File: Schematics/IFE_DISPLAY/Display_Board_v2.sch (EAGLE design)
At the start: 55 parts, among them IC2 EP2C5T144, Q1 16MHz, Q3 16MHz, U2 EPCS1SI8N, U3 ATMEGA328P-AU, U4 HEX_CONVERTER, U5 HEX_CONVERTER, U6 MC78LC33NTRG, U7 MC78LC50NTRG

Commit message: adding linear regs
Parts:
- removed AS1, JTAG1: (no value), pinhead:PINHD-2X5
- removed C24: 220u, Capacitors:C1206
- removed R27, R28, R33: 1K, resistor:R-US_R0805
- removed U6: MC78LC33NTRG, ON Semiconductor_By_element14_Batch_1:MC78LC33NTRG
- removed U7: MC78LC50NTRG, ON Semiconductor_By_element14_Batch_1:MC78LC50NTRG
- added AS2, JTAG2: (no value), pinhead:PINHD-2X5
- added QG1: SM77H, crystal:SM77H
- added R11, R12, R2: 1K, resistor:R-US_R0805
- added R13, R14, R15, R16: 10K, resistor:R-US_R0805
- added U$6: 10CL006ZE144, Display_Custom:10CL006ZE144
- added U$7: EPCQ16A, Display_Custom:EPCQ16A
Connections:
- new net N$10: R13.1, U$6.NSTATUS
- new net N$11: U$6.VCC_PLL1@37, U$6.VCC_PLL2@109
- new net N$12: U$6.DCLK
- new net N$14: U$6.DATA1,ASDO
- new net N$15: U$6.MSEL0
- new net N$8: U$6.MSEL2
- new net N$9: U$6.VCCA1@35, U$6.VCCA2@107
- net +12V: no longer C24.1, U6.VIN, U7.VIN
- net +3V3: now also AS2.4, JTAG2.4, QG1.VCC, R11.1, R12.2, R13.2, R14.2, R15.2, U$6.VCC@117, U$6.VCC@122, U$6.VCC@130, U$6.VCC@139, U$6.VCC@17, U$6.VCC@26, U$6.VCC@40, U$6.VCC@47, U$6.VCC@56, U$6.VCC@62, U$6.VCC@81, U$6.VCC@93, U$7.VCC; no longer AS1.4, JTAG1.4, R28.1, R33.2, U6.VOUT
- net +5V: no longer U7.VOUT
- net 50_MHZ: now also QG1.OUT, U$6.CLK0
- net ASDO: now also AS2.9, U$7.DATA1; no longer AS1.9
- net CONF_DONE: now also AS2.3, R15.1, U$6.CONF_DONE; no longer AS1.3
- net DATA0: now also AS2.7, U$7.DATA0; no longer AS1.7
- net DCLK: now also AS2.1, U$7.DCLK; no longer AS1.1
- net GND: now also AS2.10, AS2.2, JTAG2.10, JTAG2.2, QG1.GND, R16.2, R2.1, U$6.GND@104, U$6.GND@108, U$6.GND@110, U$6.GND@118, U$6.GND@123, U$6.GND@131, U$6.GND@140, U$6.GND@19, U$6.GND@27, U$6.GND@30, U$6.GND@36, U$6.GND@4, U$6.GND@41, U$6.GND@48, U$6.GND@57, U$6.GND@63, U$6.GND@64, U$6.GND@79, U$6.GND@82, U$6.GND@95, U$6.MSEL1, U$7.GND; no longer AS1.10, AS1.2, C24.2, JTAG1.10, JTAG1.2, R27.1, U6.GND, U7.GND
- net NCE: now also AS2.6, R16.1, U$6.NCE; no longer AS1.6
- net NCONFIG: now also AS2.5, R14.1, U$6.NCONFIG; no longer AS1.5
- net NCSO: now also AS2.8, U$6.FLASH_NCE,NCSO, U$7.NCS; no longer AS1.8
- net TCK: now also JTAG2.1, R2.2; no longer JTAG1.1, R27.2
- net TDI: now also JTAG2.9, R11.2; no longer JTAG1.9, R28.2
- net TDO: now also JTAG2.3; no longer JTAG1.3
- net TMS: now also JTAG2.5, R12.1; no longer JTAG1.5, R33.1
- net VCC: now also U$6.VINT@102, U$6.VINT@116, U$6.VINT@134, U$6.VINT@29, U$6.VINT@45, U$6.VINT@5, U$6.VINT@61, U$6.VINT@78

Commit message: Working on adding 2.5V for the PLL
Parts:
- added U$8: LF33ABDT-TR, Display_Custom:LF33ABDT-TR
- added U$9: L7805CDT-TR, Display_Custom:L7805CDT-TR
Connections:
- net +12V: now also U$8.VIN, U$9.VIN
- net +3V3: now also U$8.VOUT
- net +5V: now also U$9.VOUT
- net GND: now also U$8.GND, U$9.GND
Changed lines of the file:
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@@
 <?xml version="1.0" encoding="utf-8"?>
 <!DOCTYPE eagle SYSTEM "eagle.dtd">
-<eagle version="8.6.0">
+<eagle version="8.6.3">
 <drawing>
 <settings>
@@
 <part name="GND22" library="supply1" library_urn="urn:adsk.eagle:library:371" deviceset="GND" device=""/>
 <part name="ANDREWSMITH" library="frames" library_urn="urn:adsk.eagle:library:229" deviceset="A3L-LOC" device=""/>
+<part name="U$8" library="Display_Custom" deviceset="LF33ABDT-TR" device=""/>
+<part name="U$9" library="Display_Custom" deviceset="L7805CDT-TR" device=""/>
 </parts>
 <sheets>
@@
 <instance part="R3" gate="G$1" x="99.06" y="157.48" rot="R90"/>
 <instance part="P+1" gate="1" x="88.9" y="177.8"/>
+<instance part="U$8" gate="LF33ABDT" x="45.72" y="114.3"/>
+<instance part="U$9" gate="L7805" x="132.08" y="114.3"/>
 </instances>
 <busses>
@@
 </segment>
 <segment>
-<wire x1="114.3" y1="104.14" x2="109.22" y2="104.14" width="0.1524" layer="91"/>
 <wire x1="109.22" y1="104.14" x2="109.22" y2="101.6" width="0.1524" layer="91"/>
 <pinref part="GND14" gate="1" pin="GND"/>
@@
 <wire x1="109.22" y1="106.68" x2="109.22" y2="104.14" width="0.1524" layer="91"/>
 <junction x="109.22" y="104.14"/>
+<wire x1="132.08" y1="106.68" x2="132.08" y2="104.14" width="0.1524" layer="91"/>
+<wire x1="132.08" y1="104.14" x2="109.22" y2="104.14" width="0.1524" layer="91"/>
+<pinref part="U$9" gate="L7805" pin="GND"/>
 </segment>
 <segment>
@@
 <wire x1="22.86" y1="106.68" x2="22.86" y2="104.14" width="0.1524" layer="91"/>
 <wire x1="22.86" y1="104.14" x2="22.86" y2="101.6" width="0.1524" layer="91"/>
-<wire x1="27.94" y1="104.14" x2="22.86" y2="104.14" width="0.1524" layer="91"/>
 <junction x="22.86" y="104.14"/>
 <pinref part="GND20" gate="1" pin="GND"/>
+<wire x1="22.86" y1="104.14" x2="45.72" y2="104.14" width="0.1524" layer="91"/>
+<pinref part="U$8" gate="LF33ABDT" pin="GND"/>
+<wire x1="45.72" y1="104.14" x2="45.72" y2="106.68" width="0.1524" layer="91"/>
 </segment>
 <segment>
@@
 <net name="+3V3" class="0">
 <segment>
-<wire x1="63.5" y1="116.84" x2="68.58" y2="116.84" width="0.1524" layer="91"/>
 <pinref part="C12" gate="G$1" pin="1"/>
 <wire x1="68.58" y1="116.84" x2="68.58" y2="114.3" width="0.1524" layer="91"/>
@@
 <junction x="68.58" y="116.84"/>
 <pinref part="+3V3" gate="G$1" pin="+3V3"/>
+<pinref part="U$8" gate="LF33ABDT" pin="VOUT"/>
+<wire x1="68.58" y1="116.84" x2="58.42" y2="116.84" width="0.1524" layer="91"/>
 </segment>
 </net>
@@
 <segment>
 <pinref part="P+4" gate="1" pin="+5V"/>
-<wire x1="149.86" y1="116.84" x2="154.94" y2="116.84" width="0.1524" layer="91"/>
 <wire x1="154.94" y1="116.84" x2="154.94" y2="119.38" width="0.1524" layer="91"/>
 <pinref part="C5" gate="G$1" pin="1"/>
 <wire x1="154.94" y1="116.84" x2="154.94" y2="114.3" width="0.1524" layer="91"/>
 <junction x="154.94" y="116.84"/>
+<wire x1="144.78" y1="116.84" x2="154.94" y2="116.84" width="0.1524" layer="91"/>
+<pinref part="U$9" gate="L7805" pin="VOUT"/>
 </segment>
 <segment>
@@
 </segment>
 <segment>
-<wire x1="27.94" y1="116.84" x2="22.86" y2="116.84" width="0.1524" layer="91"/>
 <pinref part="C11" gate="G$1" pin="1"/>
 <wire x1="22.86" y1="116.84" x2="17.78" y2="116.84" width="0.1524" layer="91"/>
@@
 <pinref part="SUPPLY2" gate="+12V" pin="+12V"/>
 <wire x1="17.78" y1="119.38" x2="17.78" y2="116.84" width="0.1524" layer="91"/>
-</segment>
-<segment>
-<wire x1="114.3" y1="116.84" x2="109.22" y2="116.84" width="0.1524" layer="91"/>
+<pinref part="U$8" gate="LF33ABDT" pin="VIN"/>
+<wire x1="33.02" y1="116.84" x2="22.86" y2="116.84" width="0.1524" layer="91"/>
+</segment>
+<segment>
 <pinref part="C10" gate="G$1" pin="1"/>
 <wire x1="109.22" y1="116.84" x2="109.22" y2="114.3" width="0.1524" layer="91"/>
@@
 <pinref part="SUPPLY1" gate="+12V" pin="+12V"/>
 <wire x1="104.14" y1="119.38" x2="104.14" y2="116.84" width="0.1524" layer="91"/>
-</segment>
-<segment>
+<wire x1="109.22" y1="116.84" x2="119.38" y2="116.84" width="0.1524" layer="91"/>
+<pinref part="U$9" gate="L7805" pin="VIN"/>
+</segment>
+<segment>

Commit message: Finished power dist - Working on optimizing connections to FPGA
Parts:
- removed AS2, JTAG2: (no value), pinhead:PINHD-2X5
- removed IC2: EP2C5T144, altera-cyclone-II:EP2C5T144
- removed JP1: (no value), pinhead:PINHD-2X3
- removed LED1, LED2, LED3: (no value), led:LEDCHIP-LED0805
- removed QG1, QG2: SM77H, crystal:SM77H
- removed R29, R30, R31, R32: 10K, resistor:R-US_R0805
- removed U$1: 776280-1, IFE_AMPSEAL_Conn:776280-1
- removed U$4: ZIF40_0.5MM_PITCH, Connectors:ZIF40_0.5MM_PITCH
- removed U2: EPCS1SI8N, Altera_By_element14_Batch_1:EPCS1SI8N
- removed U3: ATMEGA328P-AU, Atmel_By_element14_Batch_1-00:ATMEGA328P-AU
- added 1.2T, 2.5T, 3.3T, 5T, DISP_A_T: TPTP12SQ, testpad:TPTP12SQ
- added 3.3V, 5V, FPGA, MICRO: (no value), led:LEDCHIP-LED0805
- added 50MHZ: SM77H, crystal:SM77H
- added AS, JTAG: (no value), pinhead:PINHD-2X5
- added ATMEGA328P: ATMEGA328P-AU, Atmel_By_element14_Batch_1-00:ATMEGA328P-AU
- added C14: 10u, rcl:C-EUC0805K
- added C15, C18, C19, C20, C21, C22, C23: 0.1u, rcl:C-EUC0805K
- added C16: 220uF, rcl:CPOL-USUD-6,3X7,7
- added C17: 1u, rcl:C-EUC0805K
- added DISPLAY: ZIF40_0.5MM_PITCH, Connectors:ZIF40_0.5MM_PITCH
- added ICP: (no value), pinhead:PINHD-2X3
- added R17: 127k, rcl:R-US_R0805
- added R18: 121k, rcl:R-US_R0805
- added R19: 25, rcl:R-US_R0805
- added R20: 330, resistor:R-US_R0805
- added TE_AMPSEAL_8: 776280-1, IFE_AMPSEAL_Conn:776280-1
- added U$10: TPS72101DBVT, Display_Custom:TPS72101DBVT
- added U$11: TPS6104X, Display_Custom:TPS6104X
- added U$13: SMAZ24-13-F, Display_Custom:SMAZ24-13-F
- added U$14: BAT54WS-7-F, Display_Custom:BAT54WS-7-F
- C1: value 1uF -> 0.1u
- C10, C11: value 0.1u -> 10u
- C13: value 10uF -> 10u; device microbuilder:CAP_CERAMIC_0805MP -> rcl:C-EUC0805K
- C2: value 1uF -> 10u
- L1: value 6.8uH power L CID 2276 -> 6.8uH
- R3: value 10K -> 10k; device microbuilder:RESISTOR_0805MP -> rcl:R-US_R0805
- R5: value 100 -> 330
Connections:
- removed net N$14: U$6.DATA1,ASDO
- removed net N$15: U$6.MSEL0
- removed net N$21: IC2.NSTATUS, R29.1
- removed net PWR_IN_24: U$1.6
- new net N$19: R17.2, R18.1, U$10.N/C
- new net V+: 2.5T.TP, C15.1, R17.1, U$10.VOUT, U$6.MSEL0, U$6.MSEL2
- net +12V: now also C16.+
- net +3V3: now also 3.3T.TP, 50MHZ.VCC, AS.4, C18.1, C19.1, C20.1, DISPLAY.P$4, JTAG.4; no longer AS2.4, IC2.VCC@1, IC2.VCC@10, IC2.VCC@11, IC2.VCC@12, IC2.VCC@13, IC2.VCC@16, IC2.VCC@18, IC2.VCC@2, IC2.VCC@20, IC2.VCC@3, IC2.VCC@6, IC2.VCC@8, JTAG2.4, QG1.VCC, QG2.VCC, R29.2, R31.2, R32.2, R5.2, U$4.P$4, U2.VCC, U2.VCC_2, U2.VCC_3
- net +5V: now also 5T.TP, ATMEGA328P.AVCC, ATMEGA328P.VCC, ATMEGA328P.VCC_2, C14.1, ICP.2, R20.2, R3.1, R5.2, U$10.ENABLE, U$10.VIN, U$11.VIN; no longer JP1.2, R3.2, U3.AVCC, U3.VCC, U3.VCC_2
- net 50_MHZ: now also 50MHZ.OUT; no longer IC2.CLK0, QG1.OUT, QG2.OUT
- net ASDO: now also AS.9, U$6.DATA1,ASDO; no longer AS2.9, IC2.IO1, U2.ASDI
- net BLUE_0: now also DISPLAY.P$21, U$6.IO54; no longer IC2.IO52, U$4.P$21
- net BLUE_1: now also DISPLAY.P$22, U$6.IO55; no longer IC2.IO53, U$4.P$22
- net BLUE_2: now also DISPLAY.P$23, U$6.IO58; no longer IC2.IO55, U$4.P$23
- net BLUE_3: now also DISPLAY.P$24, U$6.IO59; no longer IC2.IO57, U$4.P$24
- net BLUE_4: now also DISPLAY.P$25, U$6.IO60; no longer IC2.IO58, U$4.P$25
- net BLUE_5: now also DISPLAY.P$26, U$6.IO65; no longer IC2.IO59, U$4.P$26
- net BLUE_6: now also DISPLAY.P$27, U$6.IO66; no longer IC2.IO60, U$4.P$27
- net BLUE_7: now also DISPLAY.P$28, U$6.IO67; no longer IC2.IO63, U$4.P$28
- net CANH: now also TE_AMPSEAL_8.5; no longer U$1.5
- net CANL: now also TE_AMPSEAL_8.8; no longer U$1.8
- net CONF_DONE: now also AS.3; no longer AS2.3, IC2.CONF_DONE, R32.1
- net DATA0: now also AS.7, U$6.DATA0; no longer AS2.7, IC2.DATA0, U2.DATA
- net DCLK: now also AS.1, U$6.DCLK; no longer AS2.1, IC2.DCLK, U2.DCLK
- net DISP_CLK: now also DISPLAY.P$30, U$6.IO68; no longer IC2.IO3, U$4.P$30
- net DISP_DEN: now also DISPLAY.P$34, U$6.IO72; no longer IC2.IO9, U$4.P$34
- net DISP_EN: now also DISPLAY.P$31, U$6.IO69; no longer IC2.IO4, U$4.P$31
- net DISP_HSYNC: now also DISPLAY.P$32, U$6.IO70; no longer IC2.IO7, U$4.P$32
- net DISP_LEDA: now also C17.1, DISPLAY.P$2, DISP_A_T.TP, U$13.C, U$14.C; no longer U$4.P$2
- net DISP_LEDK: now also DISPLAY.P$1, R19.1, U$11.FB; no longer U$4.P$1
- net DISP_PWM: now also ATMEGA328P.PB1, R3.2, U$11.ENABLE; no longer R3.1, U3.PB1
- net DISP_VSYNC: now also DISPLAY.P$33, U$6.IO71; no longer IC2.IO8, U$4.P$33
- net DISP_XL: now also DISPLAY.P$39, U$6.IO75; no longer U$4.P$39
- net DISP_XR: now also DISPLAY.P$37, U$6.IO73; no longer U$4.P$37
- net DISP_YD: now also DISPLAY.P$38, U$6.IO74; no longer U$4.P$38
- net DISP_YU: now also DISPLAY.P$40, U$6.IO76; no longer U$4.P$40
- net FPGA_D0_3_3: no longer IC2.IO75
- net FPGA_D1_3_3: no longer IC2.IO76
- net FPGA_D2_3_3: no longer IC2.IO79
- net FPGA_D3_3_3: no longer IC2.IO80
- net FPGA_DATA0: now also ATMEGA328P.PC0; no longer U3.PC0
- net FPGA_DATA1: now also ATMEGA328P.PC1; no longer U3.PC1
- net FPGA_DATA2: now also ATMEGA328P.PC2; no longer U3.PC2
- net FPGA_DATA3: now also ATMEGA328P.PC3; no longer U3.PC3
- net FPGA_R0_3_3: no longer IC2.IO81
- net FPGA_R1_3_3: no longer IC2.IO86
- net FPGA_R2_3_3: no longer IC2.IO87
- net FPGA_R3_3_3: no longer IC2.IO92
- net FPGA_REG0: now also ATMEGA328P.PD4; no longer U3.PD4
- net FPGA_REG1: now also ATMEGA328P.PD5; no longer U3.PD5
- net FPGA_REG2: now also ATMEGA328P.PD6; no longer U3.PD6
- net FPGA_REG3: now also ATMEGA328P.PD7; no longer U3.PD7
- net FPGA_REG_SEL: now also ATMEGA328P.PC4; no longer U3.PC4
- net FPGA_RSEL_3_3: no longer IC2.IO73
- net FPGA_WRITE: now also ATMEGA328P.PD3; no longer U3.PD3
- net FPGA_W_3_3: no longer IC2.IO74
- net GND: now also 3.3V.C, 50MHZ.GND, 5V.C, AS.10, AS.2, ATMEGA328P.GND, ATMEGA328P.GND_2, ATMEGA328P.GND_3, C14.2, C15.2, C16.-, C17.2, C18.2, C19.2, C20.2, C21.2, C22.2, C23.2, DISPLAY.P$29, DISPLAY.P$3, DISPLAY.P$36, ICP.6, JTAG.10, JTAG.2, R18.2, R19.2, TE_AMPSEAL_8.1, TE_AMPSEAL_8.3, TE_AMPSEAL_8.4, TE_AMPSEAL_8.6, TE_AMPSEAL_8.7, U$10.GND, U$11.GND, U$13.A; no longer AS2.10, AS2.2, IC2.GND@1, IC2.GND@10, IC2.GND@11, IC2.GND@12, IC2.GND@13, IC2.GND@14, IC2.GND@15, IC2.GND@16, IC2.GND@17, IC2.GND@18, IC2.GND@19, IC2.GND@2, IC2.GND@20, IC2.GND@21, IC2.GND@22, IC2.GND@23, IC2.GND@3, IC2.GND@4, IC2.GND@5, IC2.GND@6, IC2.GND@7, IC2.GND@8, IC2.GND@9, IC2.MSEL0, IC2.MSEL1, JP1.6, JTAG2.10, JTAG2.2, LED3.C, QG1.GND, QG2.GND, R30.2, U$1.4, U$4.P$29, U$4.P$3, U$4.P$36, U2.GND, U3.GND, U3.GND_2, U3.GND_3
- net GREEN_0: now also DISPLAY.P$13, U$6.IO43; no longer IC2.IO41, U$4.P$13
- net GREEN_1: now also DISPLAY.P$14, U$6.IO44; no longer IC2.IO42, U$4.P$14
- net GREEN_2: now also DISPLAY.P$15, U$6.IO46; no longer IC2.IO43, U$4.P$15
- net GREEN_3: now also DISPLAY.P$16, U$6.IO49; no longer IC2.IO44, U$4.P$16
- net GREEN_4: now also DISPLAY.P$17, U$6.IO50; no longer IC2.IO45, U$4.P$17
- net GREEN_5: now also DISPLAY.P$18, U$6.IO51; no longer IC2.IO47, U$4.P$18
- net GREEN_6: now also DISPLAY.P$19, U$6.IO52; no longer IC2.IO48, U$4.P$19
- net GREEN_7: now also DISPLAY.P$20, U$6.IO53; no longer IC2.IO51, U$4.P$20
- net LED1: now also FPGA.C, U$6.IO144; no longer IC2.IO129, LED1.C
- net LED2: now also ATMEGA328P.PB2, MICRO.C; no longer IC2.IO132, LED2.C
- net MISO: now also ATMEGA328P.PB4, ICP.1; no longer JP1.1, U3.PB4
- net MOSI: now also ATMEGA328P.PB3, ICP.4; no longer JP1.4, U3.PB3
- net N$12: now also 5V.A, R20.1; no longer U$6.DCLK
- net N$2: now also FPGA.A; no longer LED1.A
- net N$3: now also MICRO.A; no longer LED2.A
- net N$4: now also 3.3V.A; no longer LED3.A
- net N$8: now also L1.2, U$11.SW, U$14.A; no longer U$6.MSEL2
- net NCE: now also AS.6; no longer AS2.6, IC2.NCE, R30.1
- net NCONFIG: now also AS.5; no longer AS2.5, IC2.NCONFIG, R31.1
- net NCSO: now also AS.8; no longer AS2.8, IC2.IO2, U2.NCS
- net NOT_CONNECTED: now also DISPLAY.P$35; no longer U$4.P$35
- net PWR_IN_12: now also TE_AMPSEAL_8.2; no longer U$1.7
- net RED_0: now also DISPLAY.P$5, U$6.IO28; no longer IC2.IO25, U$4.P$5
- net RED_1: now also DISPLAY.P$6, U$6.IO31; no longer IC2.IO26, U$4.P$6
- net RED_2: now also DISPLAY.P$7, U$6.IO32; no longer IC2.IO27, U$4.P$7
- net RED_3: now also DISPLAY.P$8, U$6.IO33; no longer IC2.IO28, U$4.P$8
- net RED_4: now also DISPLAY.P$9, U$6.IO34; no longer IC2.IO30, U$4.P$9
- net RED_5: now also DISPLAY.P$10, U$6.IO38; no longer IC2.IO31, U$4.P$10
- net RED_6: now also DISPLAY.P$11, U$6.IO39; no longer IC2.IO32, U$4.P$11
- net RED_7: now also DISPLAY.P$12, U$6.IO42; no longer IC2.IO40, U$4.P$12
- net RESET: now also ATMEGA328P.PC6, ICP.5; no longer JP1.5, U3.PC6
- net RXD: now also ATMEGA328P.PD0; no longer U3.PD0
- net SCK: now also ATMEGA328P.PB5, ICP.3; no longer JP1.3, U3.PB5
- net TCK: now also JTAG.1, U$6.TCK; no longer IC2.TCK, JTAG2.1
- net TDI: now also JTAG.9, U$6.TDI; no longer IC2.TDI, JTAG2.9
- net TDO: now also JTAG.3, U$6.TDO; no longer IC2.TDO, JTAG2.3
- net TMS: now also JTAG.5, U$6.TMS; no longer IC2.TMS, JTAG2.5
- net TXD: now also ATMEGA328P.PD1; no longer U3.PD1
- net VCC: now also 1.2T.TP, C21.1, C22.1, C23.1; no longer IC2.VCC@14, IC2.VCC@15, IC2.VCC@17, IC2.VCC@19, IC2.VCC@4, IC2.VCC@5, IC2.VCC@7, IC2.VCC@9
- net XTAL1: now also ATMEGA328P.PB6; no longer U3.PB6
- net XTAL2: now also ATMEGA328P.PB7; no longer U3.PB7
- net ~CS_CAN: now also ATMEGA328P.PC5; no longer U3.PC5
- net ~INT_CAN: now also ATMEGA328P.PD2; no longer U3.PD2

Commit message: General Layout
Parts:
- added GND: TPTP12SQ, testpad:TPTP12SQ
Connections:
- net GND: now also GND.TP
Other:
- moved on the sheet: 1.2T, 5T, C10, C12, C18, C19, C20, C5

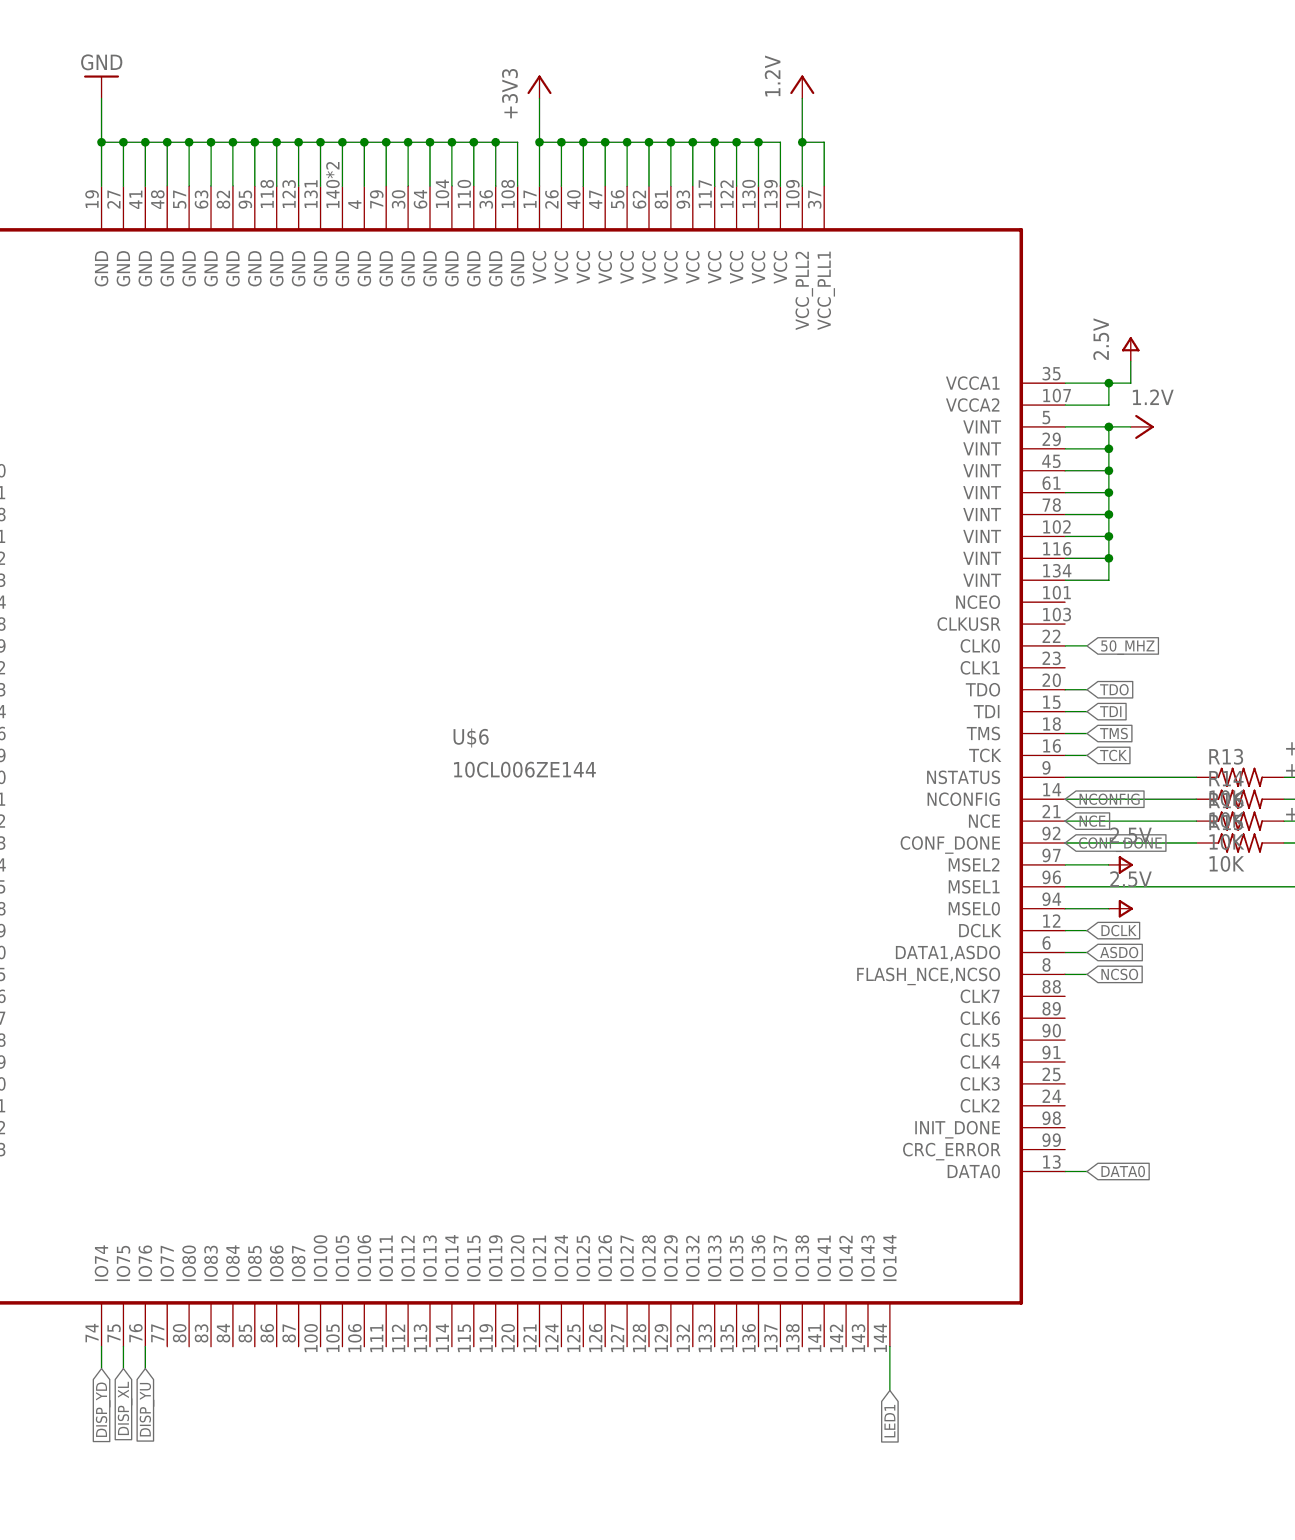
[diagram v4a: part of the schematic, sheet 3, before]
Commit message: Need to fix oscillators, Initial placement done
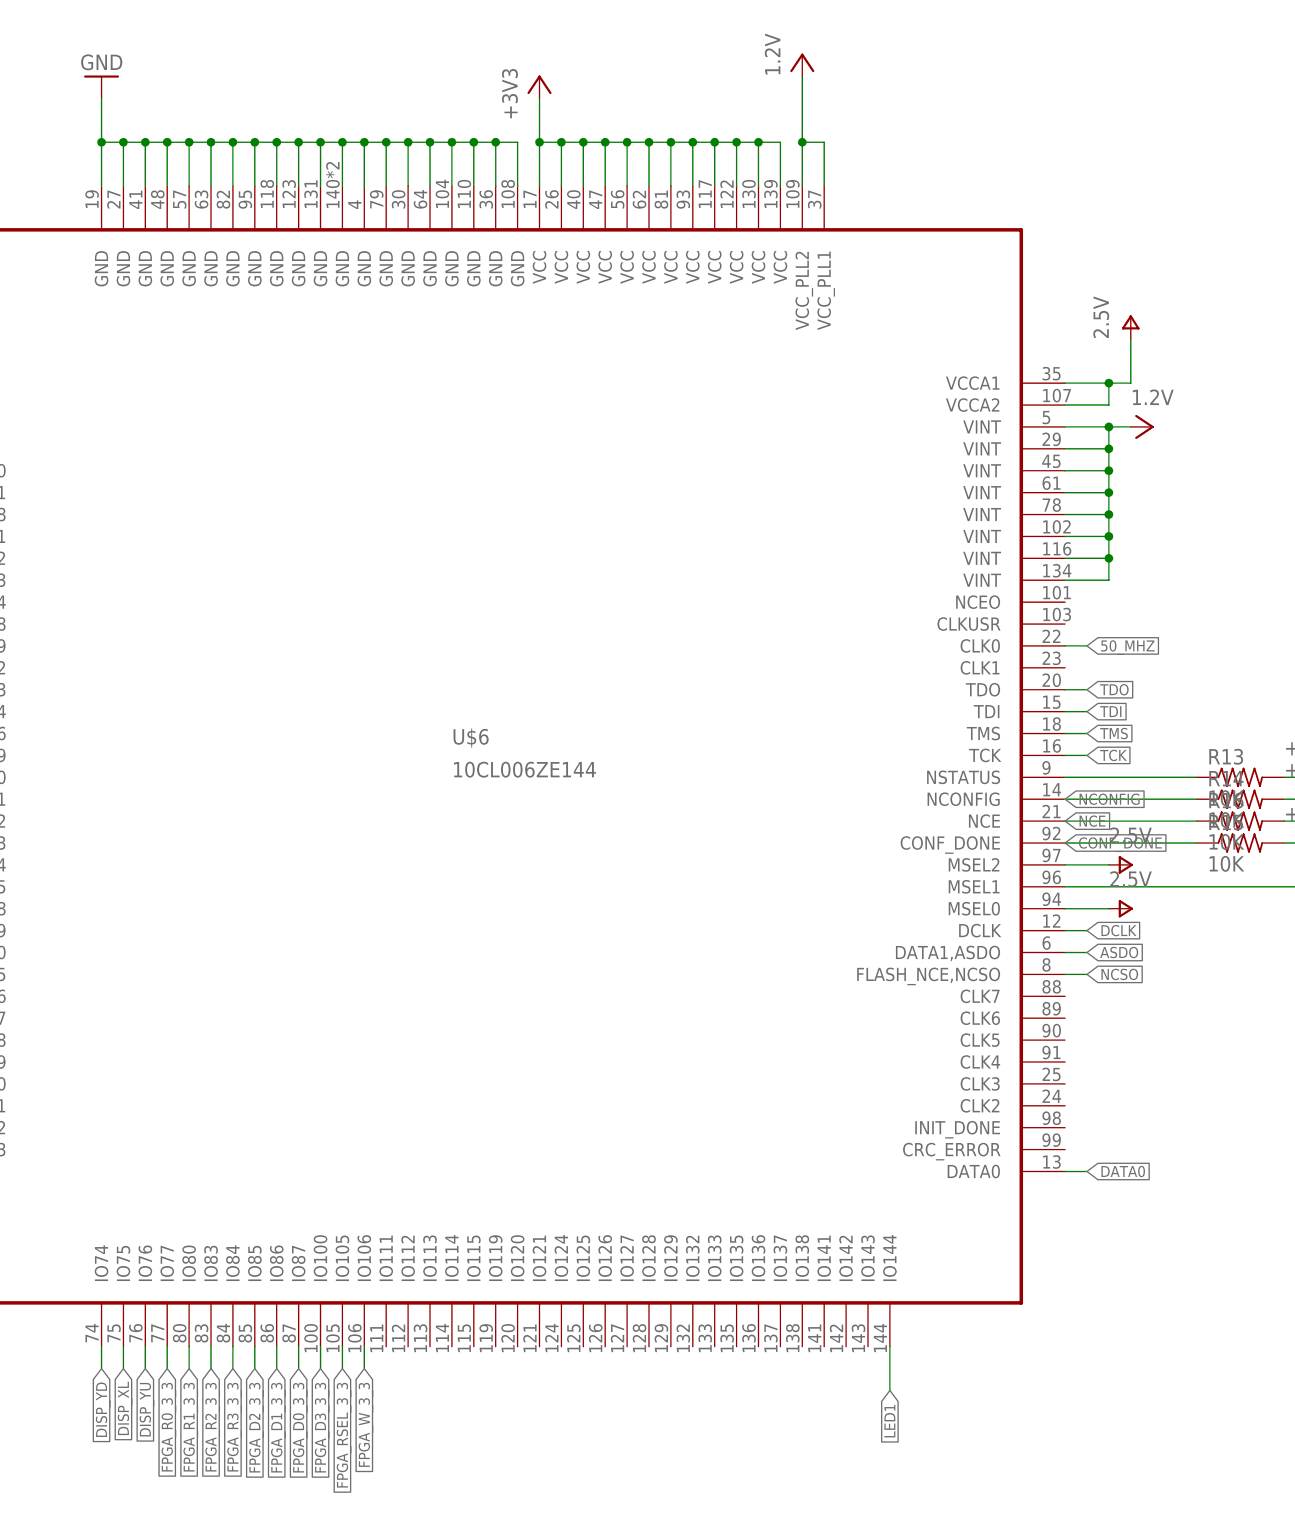
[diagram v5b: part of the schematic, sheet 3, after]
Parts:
- renumbered FUSE3 to FUSE
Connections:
- removed net N$11: U$6.VCC_PLL1@37, U$6.VCC_PLL2@109
- removed net N$9: U$6.VCCA1@35, U$6.VCCA2@107
- net FPGA_D0_3_3: now also U$6.IO87
- net FPGA_D1_3_3: now also U$6.IO86
- net FPGA_D2_3_3: now also U$6.IO85
- net FPGA_D3_3_3: now also U$6.IO100
- net FPGA_R0_3_3: now also U$6.IO77, U5.4Y; no longer U5.1Y
- net FPGA_R1_3_3: now also U$6.IO80, U5.3Y; no longer U5.2Y
- net FPGA_R2_3_3: now also U$6.IO83, U5.2Y; no longer U5.3Y
- net FPGA_R3_3_3: now also U$6.IO84, U5.1Y; no longer U5.4Y
- net FPGA_REG0: now also U5.4A; no longer U5.1A
- net FPGA_REG1: now also U5.3A; no longer U5.2A
- net FPGA_REG2: now also U5.2A; no longer U5.3A
- net FPGA_REG3: now also U5.1A; no longer U5.4A
- net FPGA_RSEL_3_3: now also U$6.IO105
- net FPGA_W_3_3: now also U$6.IO106
- net V+: now also U$6.VCCA1@35, U$6.VCCA2@107
- net VCC: now also U$6.VCC_PLL1@37, U$6.VCC_PLL2@109
